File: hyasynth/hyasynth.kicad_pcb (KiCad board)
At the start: 2 copper layers, 108 x 53 mm, 39 parts, among them J2 Conn_01x02_Male

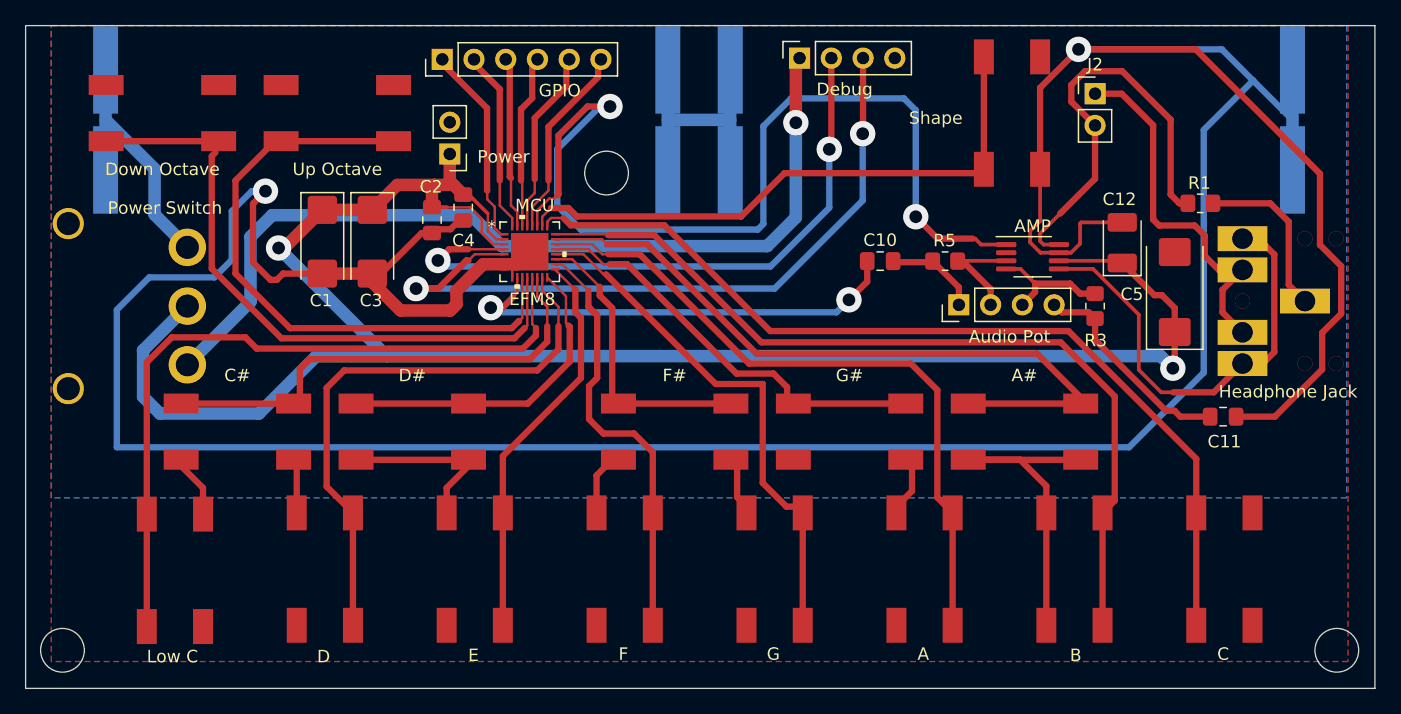
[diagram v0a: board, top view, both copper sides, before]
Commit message: New Switch and Silkscreen changes
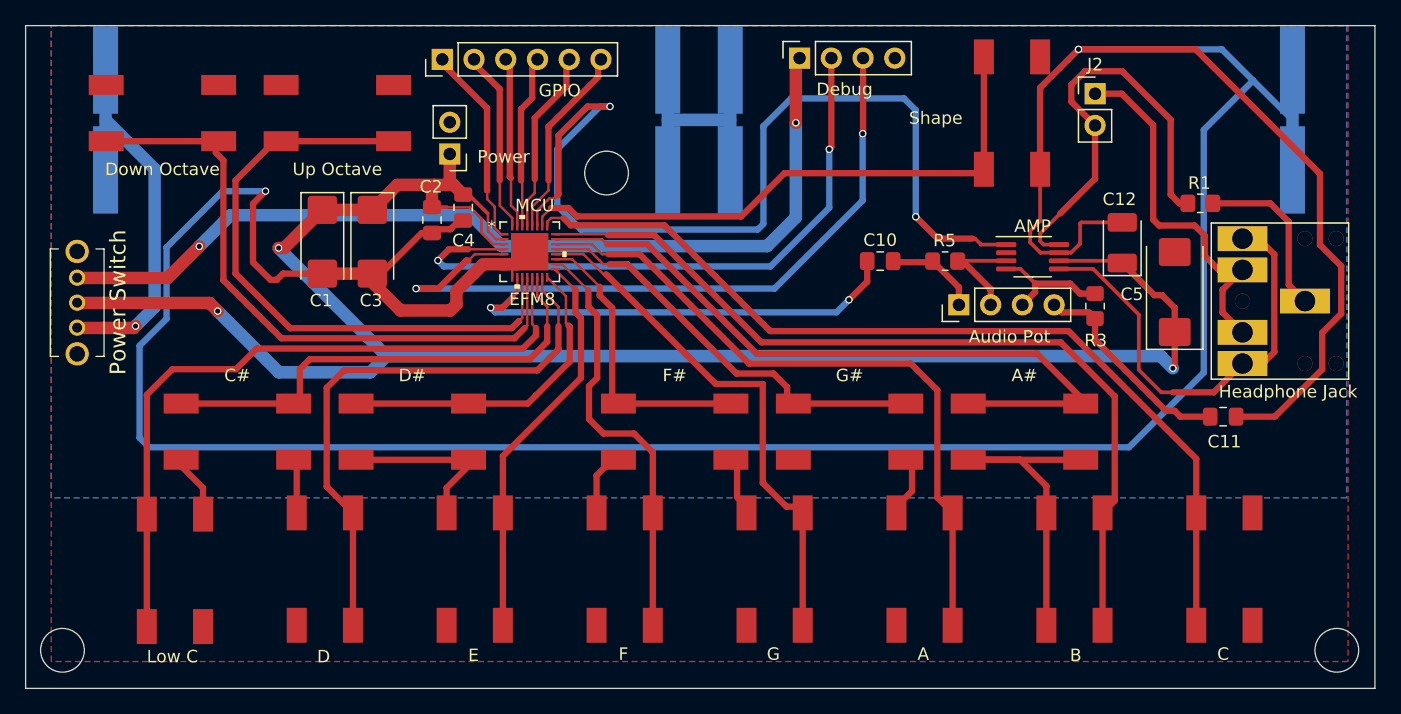
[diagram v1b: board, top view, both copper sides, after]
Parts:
- Power Switch: footprint Switch:Slide Switch -> powerSwitch:SK12D07VG4NSPA
- moved Power Switch 9.11 mm to (160.4, 50.4), turned to -90 degrees
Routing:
- net Net-(BT1-Pad1): track 12.9 -> 23.5 mm, vias 0 -> 1
- net GND: track 346.1 -> 341.4 mm
- net VDD: track 156.3 -> 153.3 mm, vias 2 -> 3
- net /Debug_Power: track 71.6 -> 74.5 mm, vias 1 -> 2
- net /Low_C: track 59.2 -> 56.9 mm

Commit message: Changes to silkscreen
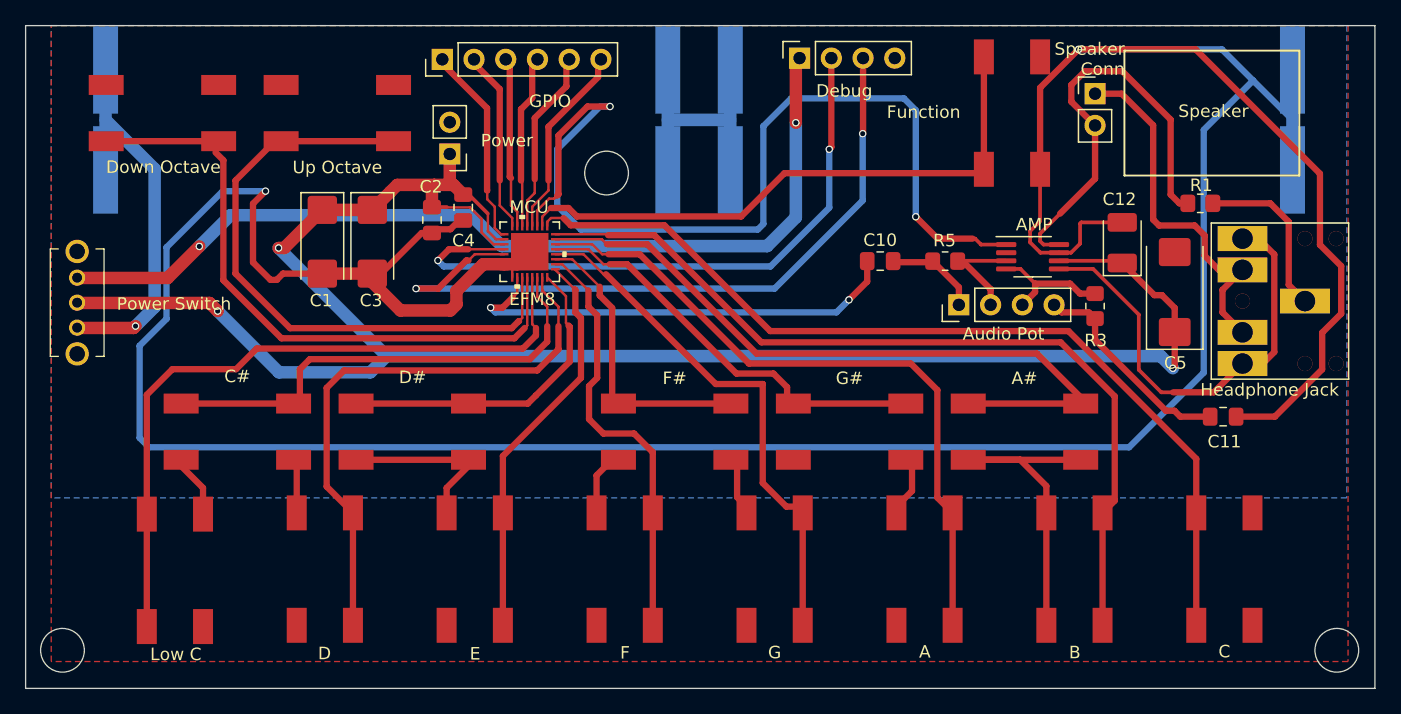
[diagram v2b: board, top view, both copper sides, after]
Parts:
- added G***: LOGO, Logo:SpringSilk, B.Cu at (253.8, 34.5)
- added G***: LOGO, Logo:SpringSilk, B.Cu at (203.7, 38.7)
- J5: renamed from Audio Pot
- J6: renamed from Headphone Jack
- SW1: renamed from Power Switch
- SW15: renamed from Down Octave
- SW17: renamed from Up Octave
- SW2: renamed from Low C
- renumbered Debug to J1, GPIO to J3, Power to J4, G# to SW10, A to SW11, A# to SW12, B to SW13, C to SW14, Shape to SW16, C# to SW3, D to SW4, D# to SW5, E to SW6, F to SW7, F# to SW8, G to SW9, MCU to U1, AMP to U3
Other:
- board text added: "+"
- board text added: "-"
- board text added: "1"
- board text added: "2"
- board text added: "3"
- board text added: "4"
- board text added: "C2CLK"
- board text added: "C2D"
- board text added: "DEBUG"
- board text added: "DEBUG POWER"
- board text added: "GND"
- board text added: "GPIO"
- board text added: "Power"
- board text added: "RX"
- board text added: "SPK +"
- board text added: "SPK -"
- board text added: "Speaker"
- board text added: "Speaker Conn"
- board text added: "TX"

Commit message: Fab 2
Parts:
- U1: value EFM8 -> EFM8LB12F64E-B-QFN32
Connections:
- net /GPIO_4 renamed /GPIO_0
- J3 pad 2: /GPIO_3 -> /GPIO_1
- J3 pad 4: /GPIO_1 -> /GPIO_3
- U1 pad 30: /GPIO_1 -> /GPIO_3
- U1 pad 32: /GPIO_3 -> /GPIO_1
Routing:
- net /GPIO_3: track 14.6 -> 13.7 mm
- net /GPIO_1: track 13.7 -> 14.6 mm
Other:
- board text added: "0"
- board text removed: "4"
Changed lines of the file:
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@@
   (net 21 "/Function")
   (net 22 "/Up")
-  (net 23 "/GPIO_4")
+  (net 23 "/GPIO_0")
   (net 24 "VDD")
   (net 25 "/DAC")
@@
       (effects (font (size 1 1) (thickness 0.15)))
     )
-    (fp_text value "EFM8" (at 0.2 3.800001) (layer "F.SilkS")
+    (fp_text value "EFM8LB12F64E-B-QFN32" (at 0.2 3.800001) (layer "F.SilkS")
       (effects (font (size 1 1) (thickness 0.15)))
     )
@@
     (fp_line (start -2 -0.73) (end -0.73 -2) (layer "F.Fab") (width 0.1))
     (pad "1" smd rect (at -2.049998 -1.4 90) (size 0.2 0.7) (layers "F.Cu" "F.Paste" "F.Mask")
-      (net 23 "/GPIO_4") (pinfunction "P0-0") (pintype "bidirectional"))
+      (net 23 "/GPIO_0") (pinfunction "P0-0") (pintype "bidirectional"))
     (pad "2" smd rect (at -2.049998 -1.000001 90) (size 0.2 0.7) (layers "F.Cu" "F.Paste" "F.Mask")
       (net 24 "VDD") (pinfunction "VIO") (pintype "bidirectional"))
@@
       (net 27 "/Uart_TX") (pinfunction "P0-4") (pintype "bidirectional"))
     (pad "30" smd rect (at -0.599999 -2.049998) (size 0.2 0.7) (layers "F.Cu" "F.Paste" "F.Mask")
-      (net 28 "/GPIO_1") (pinfunction "P0-3") (pintype "bidirectional"))
+      (net 30 "/GPIO_3") (pinfunction "P0-3") (pintype "bidirectional"))
     (pad "31" smd rect (at -1.000001 -2.049998) (size 0.2 0.7) (layers "F.Cu" "F.Paste" "F.Mask")
       (net 29 "/GPIO_2") (pinfunction "P0-2") (pintype "bidirectional"))
     (pad "32" smd rect (at -1.4 -2.049998) (size 0.2 0.7) (layers "F.Cu" "F.Paste" "F.Mask")
-      (net 30 "/GPIO_3") (pinfunction "P0-1") (pintype "bidirectional"))
+      (net 28 "/GPIO_1") (pinfunction "P0-1") (pintype "bidirectional"))
     (pad "33" smd rect (at 0 0) (size 2.999999 2.999999) (layers "F.Cu" "F.Mask")
       (net 3 "GND") (pinfunction "EPAD") (pintype "unspecified"))
@@
     (fp_line (start -0.635 -1.27) (end 1.27 -1.27) (layer "F.Fab") (width 0.1))
     (pad "1" thru_hole rect locked (at 0 0 90) (size 1.7 1.7) (drill 1) (layers *.Cu *.Mask)
-      (net 23 "/GPIO_4") (pinfunction "Pin_1") (pintype "passive"))
+      (net 23 "/GPIO_0") (pinfunction "Pin_1") (pintype "passive"))
     (pad "2" thru_hole oval locked (at 0 2.54 90) (size 1.7 1.7) (drill 1) (layers *.Cu *.Mask)
-      (net 30 "/GPIO_3") (pinfunction "Pin_2") (pintype "passive"))
+      (net 28 "/GPIO_1") (pinfunction "Pin_2") (pintype "passive"))
     (pad "3" thru_hole oval locked (at 0 5.08 90) (size 1.7 1.7) (drill 1) (layers *.Cu *.Mask)
       (net 29 "/GPIO_2") (pinfunction "Pin_3") (pintype "passive"))
     (pad "4" thru_hole oval locked (at 0 7.62 90) (size 1.7 1.7) (drill 1) (layers *.Cu *.Mask)
-      (net 28 "/GPIO_1") (pinfunction "Pin_4") (pintype "passive"))
+      (net 30 "/GPIO_3") (pinfunction "Pin_4") (pintype "passive"))
     (pad "5" thru_hole oval locked (at 0 10.16 90) (size 1.7 1.7) (drill 1) (layers *.Cu *.Mask)
       (net 27 "/Uart_TX") (pinfunction "Pin_5") (pintype "passive"))
@@
     (effects (font (size 1.5 1.5) (thickness 0.3)) (justify mirror))
   )
-  (gr_text "4" (at 189.5 35.3 90) (layer "B.SilkS")
+  (gr_text "3" (at 197.25 35.25 90) (layer "B.SilkS")
+    (effects (font (size 1.5 1.5) (thickness 0.3)) (justify mirror))
+  )
+  (gr_text "0" (at 189.5 35.3 90) (layer "B.SilkS")
     (effects (font (size 1.5 1.5) (thickness 0.3)) (justify mirror))
   )
@@
     (effects (font (size 1.5 1.5) (thickness 0.3)) (justify mirror))
   )
-  (gr_text "1" (at 197.25 35.25 90) (layer "B.SilkS")
-    (effects (font (size 1.5 1.5) (thickness 0.3)) (justify mirror))
-  )
   (gr_text "SPK +" (at 236.575 35.525) (layer "B.SilkS")
     (effects (font (size 1.5 1.5) (thickness 0.3)) (justify mirror))
@@
     (effects (font (size 1.5 1.5) (thickness 0.3)) (justify mirror))
   )
-  (gr_text "3" (at 192.1 35.225 90) (layer "B.SilkS")
+  (gr_text "1" (at 192.1 35.225 90) (layer "B.SilkS")
     (effects (font (size 1.5 1.5) (thickness 0.3)) (justify mirror))
   )
@@
   (segment (start 199.535 35.065) (end 197 37.6) (width 0.508) (layer "F.Cu") (net 27))
   (segment (start 196.4 46.250001) (end 196.4 44.2) (width 0.2) (layer "F.Cu") (net 27))
-  (segment (start 196.8 36) (end 195.9 36.9) (width 0.508) (layer "F.Cu") (net 28))
-  (segment (start 196.995 33) (end 196.8 33.195) (width 0.508) (layer "F.Cu") (net 28))
-  (segment (start 196.000001 46.250001) (end 196.000001 42.700001) (width 0.2) (layer "F.Cu") (net 28))
-  (segment (start 196.000001 42.700001) (end 195.9 42.6) (width 0.2) (layer "F.Cu") (net 28))
-  (segment (start 195.9 36.9) (end 195.9 42.6) (width 0.508) (layer "F.Cu") (net 28))
-  (segment (start 196.8 33.195) (end 196.8 36) (width 0.508) (layer "F.Cu") (net 28))
+  (segment (start 195.2 46.250001) (end 195.2 45.6) (width 0.2) (layer "F.Cu") (net 28))
+  (segment (start 194.2 35.285) (end 194.2 42.6) (width 0.508) (layer "F.Cu") (net 28))
+  (segment (start 195.2 45.6) (end 194.2 44.6) (width 0.2) (layer "F.Cu") (net 28))
+  (segment (start 191.915 33) (end 194.2 35.285) (width 0.508) (layer "F.Cu") (net 28))
+  (segment (start 194.2 44.6) (end 194.2 42.6) (width 0.2) (layer "F.Cu") (net 28))
   (segment (start 195.1 44.6) (end 195.1 42.4) (width 0.2) (layer "F.Cu") (net 29))
   (segment (start 195.599999 45.099999) (end 195.1 44.6) (width 0.2) (layer "F.Cu") (net 29))
@@
   (segment (start 194.455 33) (end 195 33.545) (width 0.508) (layer "F.Cu") (net 29))
   (segment (start 195 42.3) (end 195.1 42.4) (width 0.508) (layer "F.Cu") (net 29))
-  (segment (start 195.2 46.250001) (end 195.2 45.6) (width 0.2) (layer "F.Cu") (net 30))
-  (segment (start 194.2 35.285) (end 194.2 42.6) (width 0.508) (layer "F.Cu") (net 30))
-  (segment (start 195.2 45.6) (end 194.2 44.6) (width 0.2) (layer "F.Cu") (net 30))
-  (segment (start 191.915 33) (end 194.2 35.285) (width 0.508) (layer "F.Cu") (net 30))
-  (segment (start 194.2 44.6) (end 194.2 42.6) (width 0.2) (layer "F.Cu") (net 30))
+  (segment (start 196.8 36) (end 195.9 36.9) (width 0.508) (layer "F.Cu") (net 30))
+  (segment (start 196.995 33) (end 196.8 33.195) (width 0.508) (layer "F.Cu") (net 30))
+  (segment (start 196.000001 46.250001) (end 196.000001 42.700001) (width 0.2) (layer "F.Cu") (net 30))
+  (segment (start 196.000001 42.700001) (end 195.9 42.6) (width 0.2) (layer "F.Cu") (net 30))
+  (segment (start 195.9 36.9) (end 195.9 42.6) (width 0.508) (layer "F.Cu") (net 30))
+  (segment (start 196.8 33.195) (end 196.8 36) (width 0.508) (layer "F.Cu") (net 30))
   (segment (start 228.7625 49.1375) (end 225.775 49.1375) (width 0.508) (layer "F.Cu") (net 31))
   (segment (start 230.95 52.55) (end 230.95 51.15) (width 0.508) (layer "F.Cu") (net 31))
